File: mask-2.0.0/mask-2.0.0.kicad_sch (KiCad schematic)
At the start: 8 parts

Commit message: mask-2.0.0: basic schematic, start cleaning up the ratsnets
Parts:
- removed D?: SK6812, LED_SMD:LED_SK6812_EC15_1.5x1.5mm, symbol LED:SK6812
- added C10, C20, C21: 1uF, Capacitor_SMD:C_0603_1608Metric, symbol Device:C
- added C11, C12, C13, C14, C15, C16, C17, C18, C19, C6, C7: 100nF, Capacitor_SMD:C_0603_1608Metric, symbol Device:C
- added C2, C3: 10nF, Capacitor_SMD:C_0603_1608Metric, symbol Device:C
- added C4: 10pF, Capacitor_SMD:C_0603_1608Metric, symbol Device:C
- added C5: 10uF, Capacitor_SMD:C_0805_2012Metric, symbol Device:C
- added C8, C9: 22pF, Capacitor_SMD:C_0603_1608Metric, symbol Device:C
- added D1, D10, D11, D12, D13, D14, D15, D16, D17, D18, D19, D2, D20, D21, D22, D23, D24, D25, D26, D27, D28, D29, D3, D30, D31, D32, D33, D34, D35, D36, D37, D38, D39, D4, D40, D41, D42, D43, D44, D45, D46, D47, D48, D49, D5, D50, D51, D52, D53, D54, D55, D56, D57, D58, D59, D6, D60, D7, D8, D9: 1N4148W, Diode_SMD:D_SOD-123, symbol Diode:1N4148W
- added D61: PRTR5V0U2X, Package_TO_SOT_SMD:SOT-143, symbol Power_Protection:PRTR5V0U2X
- added D62: LED, LED_SMD:LED_0603_1608Metric, symbol Device:LED
- added FB1: 120R@550mA, Resistor_SMD:R_0603_1608Metric, symbol Device:FerriteBead
- added J2, J3: Conn_01x04, Connector_PinHeader_2.54mm:PinHeader_1x04_P2.54mm_Vertical, symbol Connector_Generic:Conn_01x04
- added R2, R3: 27, Resistor_SMD:R_0603_1608Metric, symbol Device:R
- added R4, R5: 5.1k, Resistor_SMD:R_0603_1608Metric, symbol Device:R
- added R6, R8: 10k, Resistor_SMD:R_0603_1608Metric, symbol Device:R
- added R7: 1k, Resistor_SMD:R_0603_1608Metric, symbol Device:R
- added SW1, SW10, SW11, SW12, SW13, SW14, SW15, SW16, SW17, SW18, SW19, SW2, SW20, SW21, SW22, SW23, SW24, SW25, SW26, SW27, SW28, SW29, SW3, SW30, SW31, SW32, SW33, SW34, SW35, SW36, SW37, SW38, SW39, SW4, SW40, SW41, SW42, SW43, SW44, SW45, SW46, SW47, SW48, SW49, SW5, SW50, SW51, SW52, SW53, SW54, SW55, SW56, SW57, SW58, SW59, SW6, SW60, SW7, SW8, SW9: Cherry_MX_ULP_SK6812_1515, mask:Cherry_MX_ULP_SK6812_1515, symbol mask:Cherry_MX_ULP_SK6812_1515
- added SW61, SW62: SW_Push, Button_Switch_SMD:SW_SPST_B3U-1000P, symbol Switch:SW_Push
- C1: renamed from C?; value C -> 10uF; footprint (none) -> Capacitor_SMD:C_0805_2012Metric
- R1: renamed from R?; value R -> 1k; footprint (none) -> Resistor_SMD:R_0603_1608Metric
- Y1: renamed from Y?; value Crystal -> 445C25D12M00000; Digikey https://www.digikey.at/de/products/detail/cts-frequency-controls/445C35D12M00000/3135822 -> https://www.digikey.at/de/products/detail/cts-frequency-controls/445C25D12M00000/3135096
- gave numbers to parts that had none: 4
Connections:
- net QSPI_SS: now reaches U3.1 (~{CS})
- net QSPI_SS: now also U1.56 (QSPI_SS), R6.1, R7.2
- net at U3.2 (DO(IO1)): now also U1.55 (QSPI_SD1)
- net at U3.3 (IO2): now also U1.54 (QSPI_SD2)
- net GND: now reaches U3.4 (GND)
- net GND: now also C1.2, J1.A1 (GND), J1.A12 (GND), J1.B1 (GND), J1.B12 (GND), U1.19 (TESTEN), U1.57 (GND), U2.2 (GND), C10.2, C11.2, C12.2, C13.2, C14.2, C15.2, C16.2, C17.2, C18.2, C19.2, C2.2, C20.2, C21.2, C3.2, C4.2, C5.2, C6.2, C7.2, C8.2, C9.2, D61.1 (GND), J2.4 (Pin_4), J3.4 (Pin_4), R4.2, R5.2, R8.1, SW1.1 (VSS), SW10.1 (VSS), SW11.1 (VSS), SW12.1 (VSS), SW13.1 (VSS), SW14.1 (VSS), SW15.1 (VSS), SW16.1 (VSS), SW17.1 (VSS), SW18.1 (VSS), SW19.1 (VSS), SW2.1 (VSS), SW20.1 (VSS), SW21.1 (VSS), SW22.1 (VSS), SW23.1 (VSS), SW24.1 (VSS), SW25.1 (VSS), SW26.1 (VSS), SW27.1 (VSS), SW28.1 (VSS), SW29.1 (VSS), SW3.1 (VSS), SW30.1 (VSS), SW31.1 (VSS), SW32.1 (VSS), SW33.1 (VSS), SW34.1 (VSS), SW35.1 (VSS), SW36.1 (VSS), SW37.1 (VSS), SW38.1 (VSS), SW39.1 (VSS), SW4.1 (VSS), SW40.1 (VSS), SW41.1 (VSS), SW42.1 (VSS), SW43.1 (VSS), SW44.1 (VSS), SW45.1 (VSS), SW46.1 (VSS), SW47.1 (VSS), SW48.1 (VSS), SW49.1 (VSS), SW5.1 (VSS), SW50.1 (VSS), SW51.1 (VSS), SW52.1 (VSS), SW53.1 (VSS), SW54.1 (VSS), SW55.1 (VSS), SW56.1 (VSS), SW57.1 (VSS), SW58.1 (VSS), SW59.1 (VSS), SW6.1 (VSS), SW60.1 (VSS), SW61.1, SW62.1, SW7.1 (VSS), SW8.1 (VSS), SW9.1 (VSS)
- net at U3.5 (DI(IO0)): now also U1.53 (QSPI_SD0)
- net at U3.6 (CLK): now also U1.52 (QSPI_SCLK)
- net at U3.7 (IO3): now also U1.51 (QSPI_SD3)
- net +3.3V: now reaches U3.8 (VCC)
- net +3.3V: now also U1.1 (IOVDD), U1.10 (IOVDD), U1.22 (IOVDD), U1.33 (IOVDD), U1.42 (IOVDD), U1.43 (ADC_AVDD), U1.44 (VREG_IN), U1.48 (USB_VDD), U1.49 (IOVDD), U2.5 (VOUT), C13.1, C14.1, C15.1, C16.1, C17.1, C18.1, C19.1, C20.1, C21.1, C5.1, C6.1, C7.1, D62.2 (A), J2.3 (Pin_3), J3.1 (Pin_1), R6.2, SW1.3 (VDD), SW10.3 (VDD), SW11.3 (VDD), SW12.3 (VDD), SW13.3 (VDD), SW14.3 (VDD), SW15.3 (VDD), SW16.3 (VDD), SW17.3 (VDD), SW18.3 (VDD), SW19.3 (VDD), SW2.3 (VDD), SW20.3 (VDD), SW21.3 (VDD), SW22.3 (VDD), SW23.3 (VDD), SW24.3 (VDD), SW25.3 (VDD), SW26.3 (VDD), SW27.3 (VDD), SW28.3 (VDD), SW29.3 (VDD), SW3.3 (VDD), SW30.3 (VDD), SW31.3 (VDD), SW32.3 (VDD), SW33.3 (VDD), SW34.3 (VDD), SW35.3 (VDD), SW36.3 (VDD), SW37.3 (VDD), SW38.3 (VDD), SW39.3 (VDD), SW4.3 (VDD), SW40.3 (VDD), SW41.3 (VDD), SW42.3 (VDD), SW43.3 (VDD), SW44.3 (VDD), SW45.3 (VDD), SW46.3 (VDD), SW47.3 (VDD), SW48.3 (VDD), SW49.3 (VDD), SW5.3 (VDD), SW50.3 (VDD), SW51.3 (VDD), SW52.3 (VDD), SW53.3 (VDD), SW54.3 (VDD), SW55.3 (VDD), SW56.3 (VDD), SW57.3 (VDD), SW58.3 (VDD), SW59.3 (VDD), SW6.3 (VDD), SW60.3 (VDD), SW7.3 (VDD), SW8.3 (VDD), SW9.3 (VDD)
- net at Y1.1: now also R1.1, C9.1
- net at Y1.2: now also U1.20 (XIN), C8.1
- net at R1.2: now also U1.21 (XOUT)
- net USBBOOT: now reaches U1.14 (GPIO11)
- net USBBOOT: now also R7.1, SW61.2
- net SDA: now reaches U1.15 (GPIO12)
- net SDA: now also J2.1 (Pin_1)
- net SCL: now reaches U1.16 (GPIO13)
- net SCL: now also J2.2 (Pin_2)
- net +1V1: now reaches U1.23 (DVDD), U1.50 (DVDD)
- net +1V1: now also U1.45 (VREG_VOUT), C10.1, C11.1, C12.1
- net at U1.24 (SWCLK): now also J3.2 (Pin_2)
- net at U1.25 (SWD): now also J3.3 (Pin_3)
- net nRESET: now reaches U1.26 (RUN)
- net nRESET: now also SW62.2
- net LED: now reaches U1.28 (GPIO17)
- net LED: now also SW1.2 (DIN)
- net at U1.46 (USB_DM): now also R3.1
- net at U1.47 (USB_DP): now also R2.2
- net +5V: now reaches C1.1
- net +5V: now also U2.1 (VIN), U2.3 (EN), C3.1, C4.1, FB1.2
- net VBUS: now reaches J1.A4 (VBUS), J1.A9 (VBUS), J1.B4 (VBUS), J1.B9 (VBUS)
- net VBUS: now also C2.1, D61.4 (VCC), FB1.1
- net at J1.A5 (CC1): now also R5.1
- net D+: now reaches J1.A6 (D+)
- net D+: now also J1.B6 (D+), D61.2 (I/O1), R2.1
- net D-: now reaches J1.A7 (D-)
- net D-: now also J1.B7 (D-), D61.3 (I/O2), R3.2
- net at J1.B5 (CC2): now also R4.1
- new net: D35.2 (A), SW35.6
- new net: SW57.4 (DOUT), SW58.2 (DIN)
- new net: SW58.4 (DOUT), SW59.2 (DIN)
- new net: D15.2 (A), SW15.6
- new net: SW59.4 (DOUT), SW60.2 (DIN)
- new net: SW53.4 (DOUT), SW54.2 (DIN)
- new net: SW54.4 (DOUT), SW55.2 (DIN)
- new net: D50.2 (A), SW50.6
- new net: D6.2 (A), SW6.6
- new net: D12.2 (A), SW12.6
- new net: SW11.4 (DOUT), SW12.2 (DIN)
- new net: SW12.4 (DOUT), SW13.2 (DIN)
- new net: D57.2 (A), SW57.6
- new net: SW38.4 (DOUT), SW39.2 (DIN)
- new net: SW39.4 (DOUT), SW40.2 (DIN)
- new net: D53.2 (A), SW53.6
- new net: D52.2 (A), SW52.6
- new net: SW5.4 (DOUT), SW6.2 (DIN)
- new net: SW6.4 (DOUT), SW7.2 (DIN)
- new net: SW33.4 (DOUT), SW34.2 (DIN)
- new net: SW34.4 (DOUT), SW35.2 (DIN)
- new net: D17.2 (A), SW17.6
- new net: SW18.4 (DOUT), SW19.2 (DIN)
- new net: SW19.4 (DOUT), SW20.2 (DIN)
- new net: SW22.4 (DOUT), SW23.2 (DIN)
- new net: SW23.4 (DOUT), SW24.2 (DIN)
- new net: SW21.4 (DOUT), SW22.2 (DIN)
- new net: D29.2 (A), SW29.6
- new net: D1.2 (A), SW1.6
- new net: D14.2 (A), SW14.6
- new net: D22.2 (A), SW22.6
- new net: D28.2 (A), SW28.6
- new net: D40.2 (A), SW40.6
- new net: D36.2 (A), SW36.6
- new net: D16.2 (A), SW16.6
- new net: SW10.4 (DOUT), SW11.2 (DIN)
- new net: SW28.4 (DOUT), SW29.2 (DIN)
- new net: SW29.4 (DOUT), SW30.2 (DIN)
- new net: SW1.4 (DOUT), SW2.2 (DIN)
- new net: SW2.4 (DOUT), SW3.2 (DIN)
- new net: D3.2 (A), SW3.6
- new net: SW41.4 (DOUT), SW42.2 (DIN)
- new net: SW42.4 (DOUT), SW43.2 (DIN)
- new net: SW37.4 (DOUT), SW38.2 (DIN)
- new net: D24.2 (A), SW24.6
- new net: SW24.4 (DOUT), SW25.2 (DIN)
- new net: SW25.4 (DOUT), SW26.2 (DIN)
- new net: SW30.4 (DOUT), SW31.2 (DIN)
- new net: SW31.4 (DOUT), SW32.2 (DIN)
- new net: SW51.4 (DOUT), SW52.2 (DIN)
- new net: SW52.4 (DOUT), SW53.2 (DIN)
- new net: D7.2 (A), SW7.6
- new net: D43.2 (A), SW43.6
- new net: SW49.4 (DOUT), SW50.2 (DIN)
- new net: SW50.4 (DOUT), SW51.2 (DIN)
- new net: SW55.4 (DOUT), SW56.2 (DIN)
- new net: SW56.4 (DOUT), SW57.2 (DIN)
- new net: D62.1 (K), R8.2
- new net: D26.2 (A), SW26.6
- new net: D10.2 (A), SW10.6
- new net: D8.2 (A), SW8.6
- new net: D25.2 (A), SW25.6
- new net: D23.2 (A), SW23.6
- new net: D38.2 (A), SW38.6
- new net: D4.2 (A), SW4.6
- new net: D33.2 (A), SW33.6
- new net: D45.2 (A), SW45.6
- new net: SW35.4 (DOUT), SW36.2 (DIN)
- new net: D56.2 (A), SW56.6
- new net: SW48.4 (DOUT), SW49.2 (DIN)
- new net: D13.2 (A), SW13.6
- new net: D27.2 (A), SW27.6
- new net: D34.2 (A), SW34.6
- new net: D20.2 (A), SW20.6
- new net: D51.2 (A), SW51.6
- new net: D11.2 (A), SW11.6
- new net: D21.2 (A), SW21.6
- new net: SW26.4 (DOUT), SW27.2 (DIN)
- new net: SW27.4 (DOUT), SW28.2 (DIN)
- new net: SW45.4 (DOUT), SW46.2 (DIN)
- new net: SW46.4 (DOUT), SW47.2 (DIN)
- new net: SW7.4 (DOUT), SW8.2 (DIN)
- new net: D5.2 (A), SW5.6
- new net: SW8.4 (DOUT), SW9.2 (DIN)
- new net: SW10.2 (DIN), SW9.4 (DOUT)
- new net: D48.2 (A), SW48.6
- new net: D30.2 (A), SW30.6
- new net: SW43.4 (DOUT), SW44.2 (DIN)
- new net: SW44.4 (DOUT), SW45.2 (DIN)
- new net: D31.2 (A), SW31.6
- new net: D9.2 (A), SW9.6
- new net: SW16.4 (DOUT), SW17.2 (DIN)
- new net: SW17.4 (DOUT), SW18.2 (DIN)
- new net: SW3.4 (DOUT), SW4.2 (DIN)
- new net: D32.2 (A), SW32.6
- new net: D2.2 (A), SW2.6
- new net: D41.2 (A), SW41.6
- new net: D37.2 (A), SW37.6
- new net: D47.2 (A), SW47.6
- new net: SW20.4 (DOUT), SW21.2 (DIN)
- new net: SW40.4 (DOUT), SW41.2 (DIN)
- new net: D54.2 (A), SW54.6
- new net: D19.2 (A), SW19.6
- new net: D49.2 (A), SW49.6
- new net: D44.2 (A), SW44.6
- new net: D55.2 (A), SW55.6
- new net: SW13.4 (DOUT), SW14.2 (DIN)
- new net: D18.2 (A), SW18.6
- new net: D39.2 (A), SW39.6
- new net: D59.2 (A), SW59.6
- new net: SW36.4 (DOUT), SW37.2 (DIN)
- new net: SW47.4 (DOUT), SW48.2 (DIN)
- new net: D60.2 (A), SW60.6
- new net: SW14.4 (DOUT), SW15.2 (DIN)
- new net: D42.2 (A), SW42.6
- new net: SW32.4 (DOUT), SW33.2 (DIN)
- new net: D46.2 (A), SW46.6
- new net: SW15.4 (DOUT), SW16.2 (DIN)
- new net: D58.2 (A), SW58.6
- new net: SW4.4 (DOUT), SW5.2 (DIN)
- new net COL0: SW1.5, SW13.5, SW25.5, SW37.5, SW49.5
- new net COL1: SW14.5, SW2.5, SW26.5, SW38.5, SW50.5
- new net COL10: SW11.5, SW23.5, SW35.5, SW47.5, SW59.5
- new net COL11: SW12.5, SW24.5, SW36.5, SW48.5, SW60.5
- new net COL2: SW15.5, SW27.5, SW3.5, SW39.5, SW51.5
- new net COL3: SW16.5, SW28.5, SW4.5, SW40.5, SW52.5
- new net COL4: SW17.5, SW29.5, SW41.5, SW5.5, SW53.5
- new net COL5: SW18.5, SW30.5, SW42.5, SW54.5, SW6.5
- new net COL6: SW19.5, SW31.5, SW43.5, SW55.5, SW7.5
- new net COL7: SW20.5, SW32.5, SW44.5, SW56.5, SW8.5
- new net COL8: SW21.5, SW33.5, SW45.5, SW57.5, SW9.5
- new net COL9: SW10.5, SW22.5, SW34.5, SW46.5, SW58.5
- new net ROW0: D1.1 (K), D10.1 (K), D11.1 (K), D12.1 (K), D2.1 (K), D3.1 (K), D4.1 (K), D5.1 (K), D6.1 (K), D7.1 (K), D8.1 (K), D9.1 (K)
- new net ROW1: D13.1 (K), D14.1 (K), D15.1 (K), D16.1 (K), D17.1 (K), D18.1 (K), D19.1 (K), D20.1 (K), D21.1 (K), D22.1 (K), D23.1 (K), D24.1 (K)
- new net ROW2: D25.1 (K), D26.1 (K), D27.1 (K), D28.1 (K), D29.1 (K), D30.1 (K), D31.1 (K), D32.1 (K), D33.1 (K), D34.1 (K), D35.1 (K), D36.1 (K)
- new net ROW3: D37.1 (K), D38.1 (K), D39.1 (K), D40.1 (K), D41.1 (K), D42.1 (K), D43.1 (K), D44.1 (K), D45.1 (K), D46.1 (K), D47.1 (K), D48.1 (K)
- new net ROW4: D49.1 (K), D50.1 (K), D51.1 (K), D52.1 (K), D53.1 (K), D54.1 (K), D55.1 (K), D56.1 (K), D57.1 (K), D58.1 (K), D59.1 (K), D60.1 (K)
- no-connect marks 0 -> 3
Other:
- moved on the sheet: C1, J1, R1, U1, U2, U3, Y1

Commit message: mask-2.0.0: update to smd kb2040 variant
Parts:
- removed C10, C20, C21: 1uF, Capacitor_SMD:C_0603_1608Metric, symbol Device:C
- removed C11, C12, C13, C14, C15, C16, C17, C18, C19, C6, C7: 100nF, Capacitor_SMD:C_0603_1608Metric, symbol Device:C
- removed C3: 10nF, Capacitor_SMD:C_0603_1608Metric, symbol Device:C
- removed C4: 10pF, Capacitor_SMD:C_0603_1608Metric, symbol Device:C
- removed C5: 10uF, Capacitor_SMD:C_0805_2012Metric, symbol Device:C
- removed C8, C9: 22pF, Capacitor_SMD:C_0603_1608Metric, symbol Device:C
- removed D10, D11, D12, D19, D20, D21, D22, D23, D24, D31, D32, D33, D34, D35, D36, D43, D44, D45, D46, D47, D48, D55, D56, D57, D58, D59, D60, D7, D8, D9: 1N4148W, Diode_SMD:D_SOD-123, symbol Diode:1N4148W
- removed D61: PRTR5V0U2X, Package_TO_SOT_SMD:SOT-143, symbol Power_Protection:PRTR5V0U2X
- removed D62: LED, LED_SMD:LED_0603_1608Metric, symbol Device:LED
- removed FB1: 120R@550mA, Resistor_SMD:R_0603_1608Metric, symbol Device:FerriteBead
- removed J3: Conn_01x04, Connector_PinHeader_2.54mm:PinHeader_1x04_P2.54mm_Vertical, symbol Connector_Generic:Conn_01x04
- removed SW10, SW11, SW12, SW19, SW20, SW21, SW22, SW23, SW24, SW31, SW32, SW33, SW34, SW35, SW36, SW43, SW44, SW45, SW46, SW47, SW48, SW55, SW56, SW57, SW58, SW59, SW60, SW7, SW8, SW9: Cherry_MX_ULP_SK6812_1515, mask:Cherry_MX_ULP_SK6812_1515, symbol mask:Cherry_MX_ULP_SK6812_1515
- removed SW61: SW_Push, Button_Switch_SMD:SW_SPST_B3U-1000P, symbol Switch:SW_Push
- removed U1: RP2040, Package_DFN_QFN:QFN-56-1EP_7x7mm_P0.4mm_EP3.2x3.2mm, symbol MCU_RaspberryPi:RP2040
- removed U2: AP2112K-3.3, Package_TO_SOT_SMD:SOT-23-5, symbol Regulator_Linear:AP2112K-3.3
- removed U3: W25Q128JVPIQ, Package_SON:WSON-8-1EP_6x5mm_P1.27mm_EP3.4x4.3mm, symbol Memory_Flash:W25Q128JVS
- removed Y1: 445C25D12M00000, Crystal:Crystal_SMD_5032-2Pin_5.0x3.2mm, symbol Device:Crystal
- added J2: USB_C_Receptacle_USB2.0, Connector_USB:USB_C_Receptacle_JAE_DX07S016JA1R1500, symbol Connector:USB_C_Receptacle_USB2.0
- added JP1, JP2: SolderJumper_3_Bridged12, Jumper:SolderJumper-3_P1.3mm_Bridged12_RoundedPad1.0x1.5mm_NumberLabels, symbol Jumper:SolderJumper_3_Bridged12
- added JP3, JP4: SolderJumper_2_Open, Jumper:SolderJumper-2_P1.3mm_Open_RoundedPad1.0x1.5mm, symbol Jumper:SolderJumper_2_Open
- added SW26: SW_Push, Button_Switch_SMD:SW_SPST_B3U-1000P, symbol Switch:SW_Push
- added U1: ProMicro, mask:KB2040_SMD, symbol SofleKeyboard-rescue:ProMicro_2-Lily58-cache-Lily58_Pro-rescue
- C1: value 10uF -> 100nF; footprint Capacitor_SMD:C_0805_2012Metric -> Capacitor_SMD:C_0603_1608Metric
- C2: value 10nF -> 100nF
- D1, D2, D3, D4, D5, D6: footprint Diode_SMD:D_SOD-123 -> mask:D_SOD-123_TopBottom
- D10: renamed from D16; footprint Diode_SMD:D_SOD-123 -> mask:D_SOD-123_TopBottom
- D11: renamed from D17; footprint Diode_SMD:D_SOD-123 -> mask:D_SOD-123_TopBottom
- D12: renamed from D18; footprint Diode_SMD:D_SOD-123 -> mask:D_SOD-123_TopBottom
- D13: renamed from D25; footprint Diode_SMD:D_SOD-123 -> mask:D_SOD-123_TopBottom
- D14: renamed from D26; footprint Diode_SMD:D_SOD-123 -> mask:D_SOD-123_TopBottom
- D15: renamed from D27; footprint Diode_SMD:D_SOD-123 -> mask:D_SOD-123_TopBottom
- D16: renamed from D28; footprint Diode_SMD:D_SOD-123 -> mask:D_SOD-123_TopBottom
- D17: renamed from D29; footprint Diode_SMD:D_SOD-123 -> mask:D_SOD-123_TopBottom
- D18: renamed from D30; footprint Diode_SMD:D_SOD-123 -> mask:D_SOD-123_TopBottom
- D19: renamed from D37; footprint Diode_SMD:D_SOD-123 -> mask:D_SOD-123_TopBottom
- D20: renamed from D38; footprint Diode_SMD:D_SOD-123 -> mask:D_SOD-123_TopBottom
- D21: renamed from D39; footprint Diode_SMD:D_SOD-123 -> mask:D_SOD-123_TopBottom
- D22: renamed from D40; footprint Diode_SMD:D_SOD-123 -> mask:D_SOD-123_TopBottom
- D23: renamed from D41; footprint Diode_SMD:D_SOD-123 -> mask:D_SOD-123_TopBottom
- D24: renamed from D42; footprint Diode_SMD:D_SOD-123 -> mask:D_SOD-123_TopBottom
- D25: renamed from D49; footprint Diode_SMD:D_SOD-123 -> mask:D_SOD-123_TopBottom
- D26: renamed from D50; footprint Diode_SMD:D_SOD-123 -> mask:D_SOD-123_TopBottom
- D27: renamed from D51; footprint Diode_SMD:D_SOD-123 -> mask:D_SOD-123_TopBottom
- D28: renamed from D52; footprint Diode_SMD:D_SOD-123 -> mask:D_SOD-123_TopBottom
- D29: renamed from D53; footprint Diode_SMD:D_SOD-123 -> mask:D_SOD-123_TopBottom
- D30: renamed from D54; footprint Diode_SMD:D_SOD-123 -> mask:D_SOD-123_TopBottom
- D7: renamed from D13; footprint Diode_SMD:D_SOD-123 -> mask:D_SOD-123_TopBottom
- D8: renamed from D14; footprint Diode_SMD:D_SOD-123 -> mask:D_SOD-123_TopBottom
- D9: renamed from D15; footprint Diode_SMD:D_SOD-123 -> mask:D_SOD-123_TopBottom
- R2, R3: value 27 -> 1k
- R4: value 5.1k -> 1k
- R5: value 5.1k -> 2.2k
- R6, R8: value 10k -> 2.2k
- R7: value 1k -> 2.2k
- SW1, SW2, SW3, SW4, SW5, SW6: footprint mask:Cherry_MX_ULP_SK6812_1515 -> mask:Cherry_MX_ULP_SK6812_1515_TopBottom
- SW10: renamed from SW16; footprint mask:Cherry_MX_ULP_SK6812_1515 -> mask:Cherry_MX_ULP_SK6812_1515_TopBottom
- SW11: renamed from SW17; footprint mask:Cherry_MX_ULP_SK6812_1515 -> mask:Cherry_MX_ULP_SK6812_1515_TopBottom
- SW12: renamed from SW18; footprint mask:Cherry_MX_ULP_SK6812_1515 -> mask:Cherry_MX_ULP_SK6812_1515_TopBottom
- SW13: renamed from SW25; footprint mask:Cherry_MX_ULP_SK6812_1515 -> mask:Cherry_MX_ULP_SK6812_1515_TopBottom
- SW14: renamed from SW26; footprint mask:Cherry_MX_ULP_SK6812_1515 -> mask:Cherry_MX_ULP_SK6812_1515_TopBottom
- SW15: renamed from SW27; footprint mask:Cherry_MX_ULP_SK6812_1515 -> mask:Cherry_MX_ULP_SK6812_1515_TopBottom
- SW16: renamed from SW28; footprint mask:Cherry_MX_ULP_SK6812_1515 -> mask:Cherry_MX_ULP_SK6812_1515_TopBottom
- SW17: renamed from SW29; footprint mask:Cherry_MX_ULP_SK6812_1515 -> mask:Cherry_MX_ULP_SK6812_1515_TopBottom
- SW18: renamed from SW30; footprint mask:Cherry_MX_ULP_SK6812_1515 -> mask:Cherry_MX_ULP_SK6812_1515_TopBottom
- SW19: renamed from SW37; footprint mask:Cherry_MX_ULP_SK6812_1515 -> mask:Cherry_MX_ULP_SK6812_1515_TopBottom
- SW20: renamed from SW38; footprint mask:Cherry_MX_ULP_SK6812_1515 -> mask:Cherry_MX_ULP_SK6812_1515_TopBottom
- SW21: renamed from SW39; footprint mask:Cherry_MX_ULP_SK6812_1515 -> mask:Cherry_MX_ULP_SK6812_1515_TopBottom
- SW22: renamed from SW40; footprint mask:Cherry_MX_ULP_SK6812_1515 -> mask:Cherry_MX_ULP_SK6812_1515_TopBottom
- SW23: renamed from SW41; footprint mask:Cherry_MX_ULP_SK6812_1515 -> mask:Cherry_MX_ULP_SK6812_1515_TopBottom
- SW24: renamed from SW42; footprint mask:Cherry_MX_ULP_SK6812_1515 -> mask:Cherry_MX_ULP_SK6812_1515_TopBottom
- SW27: renamed from SW49; footprint mask:Cherry_MX_ULP_SK6812_1515 -> mask:Cherry_MX_ULP_SK6812_1515_TopBottom
- SW28: renamed from SW50; footprint mask:Cherry_MX_ULP_SK6812_1515 -> mask:Cherry_MX_ULP_SK6812_1515_TopBottom
- SW29: renamed from SW51; footprint mask:Cherry_MX_ULP_SK6812_1515 -> mask:Cherry_MX_ULP_SK6812_1515_TopBottom
- SW30: renamed from SW52; footprint mask:Cherry_MX_ULP_SK6812_1515 -> mask:Cherry_MX_ULP_SK6812_1515_TopBottom
- SW31: renamed from SW53; footprint mask:Cherry_MX_ULP_SK6812_1515 -> mask:Cherry_MX_ULP_SK6812_1515_TopBottom
- SW32: renamed from SW54; footprint mask:Cherry_MX_ULP_SK6812_1515 -> mask:Cherry_MX_ULP_SK6812_1515_TopBottom
- SW7: renamed from SW13; footprint mask:Cherry_MX_ULP_SK6812_1515 -> mask:Cherry_MX_ULP_SK6812_1515_TopBottom
- SW8: renamed from SW14; footprint mask:Cherry_MX_ULP_SK6812_1515 -> mask:Cherry_MX_ULP_SK6812_1515_TopBottom
- SW9: renamed from SW15; footprint mask:Cherry_MX_ULP_SK6812_1515 -> mask:Cherry_MX_ULP_SK6812_1515_TopBottom
- renumbered J2 to J3, SW62 to SW25
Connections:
- net +5V is gone; now on net GND: C1.1
- net USBBOOT is gone; now on net SDA: R7.1
- net +3.3V: now also J1.A4 (VBUS), J1.A9 (VBUS), J1.B4 (VBUS), J1.B9 (VBUS), R5.2, R7.2, R8.2, J2.A4 (VBUS), J2.A9 (VBUS), J2.B4 (VBUS), J2.B9 (VBUS), U1.21 (VCC)
- net GND: now also C2.1, R1.2, R2.2, J2.A1 (GND), J2.A12 (GND), J2.B1 (GND), J2.B12 (GND), SW26.1, U1.23 (GND), U1.3 (GND), U1.4 (GND); no longer C1.2, C2.2, R4.2, R5.2, R8.1
- net SCL: now also R5.1, R6.1, JP3.2 (B), JP4.2 (B), U1.6 (SCL(PD0))
- net SDA: now also R8.1, JP1.3 (B), JP2.3 (B), U1.5 (SDA(PD1))
- net nRESET: now also R3.2, R4.2, U1.22 (RST); no longer SW25.2
- net at R1.1: now also C1.2, C2.2, J1.S1 (SHIELD), R2.1, J2.S1 (SHIELD)
- net at SW7.2 (DIN): now also SW6.4 (DOUT)
- net at SW12.4 (DOUT): now also SW13.2 (DIN)
- net at SW24.4 (DOUT): now also SW27.2 (DIN)
- net at SW18.4 (DOUT): now also SW19.2 (DIN)
- net at R3.1: now also R4.1, SW25.2, SW26.2
- net at J1.A5 (CC1): no longer R5.1
- net at J1.B5 (CC2): no longer R4.1
- net D+ renamed SPLIT_DATA
- net SPLIT_DATA: now also J2.A6 (D+), J2.B6 (D+), JP1.2 (C), JP2.2 (C); no longer R2.1
- net D- renamed SPLIT_CLOCK
- net SPLIT_CLOCK: now also J2.A7 (D-), J2.B7 (D-), JP3.1 (A), JP4.1 (A); no longer R3.2
- net LED renamed ONEWIRE_LED
- net ONEWIRE_LED: now also U1.1 (TX(PD3))
- removed net QSPI_SS: R6.1, R7.2
- removed net VBUS: C2.1, J1.A4 (VBUS), J1.A9 (VBUS), J1.B4 (VBUS), J1.B9 (VBUS)
- new net SPLIT_DATA_UART: JP1.1 (A), JP2.1 (A), U1.2 (RX(PD2))
- no-connect marks 3 -> 6
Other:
- moved on the sheet: D1, D10, D11, D12, D13, D14, D15, D16, D17, D18, D19, D2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

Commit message: mask-2.0.0: first layout prototype
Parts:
- renumbered SW27 to SW25, SW28 to SW26, SW29 to SW27, SW30 to SW28, SW31 to SW29, SW32 to SW30, SW25 to SW31, SW26 to SW32
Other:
- moved on the sheet: R3, R4, SW31, SW32

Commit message: mask-2.0.0: routing halfway done, 3.3v for led's next
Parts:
- D1, D10, D11, D12, D13, D14, D15, D16, D17, D18, D19, D2, D20, D21, D22, D23, D24, D25, D26, D27, D28, D29, D3, D30, D4, D5, D6, D7, D8, D9: footprint mask:D_SOD-123_TopBottom -> mask:D_0603_1608Metric_TopBottom
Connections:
- net COL0: no longer SW25.5
- net COL1: no longer SW26.5
- net COL2: no longer SW27.5
- net COL3: no longer SW28.5
- net COL4: now also SW25.5; no longer SW29.5
- net COL5: now also SW26.5; no longer SW30.5
- net ONEWIRE_LED: now also SW6.2 (DIN); no longer SW1.2 (DIN)
- net ROW3: now also D29.1 (K), D30.1 (K)
- net ROW4: no longer D29.1 (K), D30.1 (K)
- net at SW30.4 (DOUT): now also SW28.2 (DIN)
- net at SW5.4 (DOUT): now also SW4.2 (DIN); no longer SW6.2 (DIN)
- net at SW6.4 (DOUT): now also SW5.2 (DIN); no longer SW7.2 (DIN)
- net at SW17.2 (DIN): now also SW18.4 (DOUT); no longer SW16.4 (DOUT)
- net at SW17.4 (DOUT): now also SW16.2 (DIN); no longer SW18.2 (DIN)
- net at SW2.2 (DIN): now also SW3.4 (DOUT); no longer SW1.4 (DOUT)
- net at SW2.4 (DOUT): now also SW1.2 (DIN); no longer SW3.2 (DIN)
- net at SW24.4 (DOUT): now also SW29.2 (DIN); no longer SW25.2 (DIN)
- net at SW13.2 (DIN): now also SW14.4 (DOUT); no longer SW12.4 (DOUT)
- net at SW13.4 (DOUT): now also SW19.2 (DIN); no longer SW14.2 (DIN)
- net at SW27.4 (DOUT): now also SW26.2 (DIN); no longer SW28.2 (DIN)
- net at SW28.4 (DOUT): now also SW27.2 (DIN); no longer SW29.2 (DIN)
- net at SW25.4 (DOUT): no longer SW26.2 (DIN)
- net at SW26.4 (DOUT): now also SW25.2 (DIN); no longer SW27.2 (DIN)
- net at SW15.2 (DIN): now also SW16.4 (DOUT); no longer SW14.4 (DOUT)
- net at SW15.4 (DOUT): now also SW14.2 (DIN); no longer SW16.2 (DIN)
- net at SW4.4 (DOUT): now also SW3.2 (DIN); no longer SW5.2 (DIN)
- new net: SW12.4 (DOUT), SW18.2 (DIN)
- new net: SW1.4 (DOUT), SW7.2 (DIN)
- new net COL6: SW27.5, SW29.5
- new net COL7: SW28.5, SW30.5
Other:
- moved on the sheet: D25, D26, D27, D28, D29, D30, SW10B, SW11B, SW12B, SW13B, SW14B, SW15B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

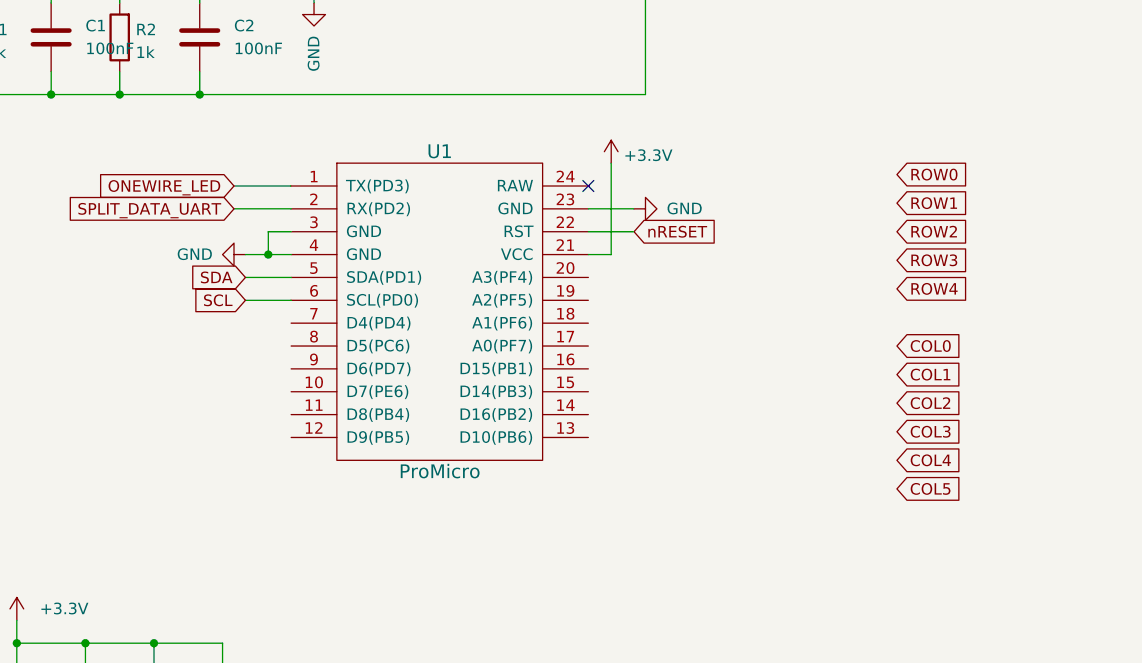
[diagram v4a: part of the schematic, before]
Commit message: mask-2.0.0: finalize routing
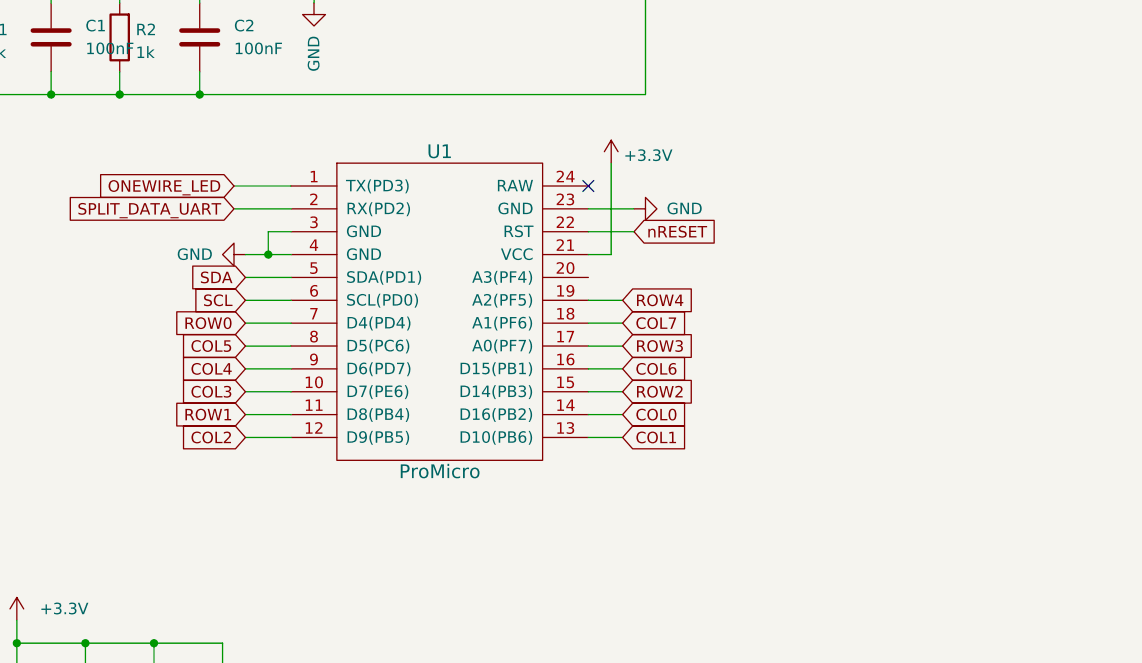
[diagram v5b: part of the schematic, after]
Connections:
- net COL0: now also U1.14 (D16(PB2))
- net COL1: now also U1.13 (D10(PB6))
- net COL2: now also U1.12 (D9(PB5))
- net COL3: now also U1.10 (D7(PE6))
- net COL4: now also U1.9 (D6(PD7))
- net COL5: now also U1.8 (D5(PC6))
- net COL6: now also U1.16 (D15(PB1))
- net COL7: now also U1.18 (A1(PF6))
- net ROW0: now also U1.7 (D4(PD4))
- net ROW1: now also U1.11 (D8(PB4))
- net ROW2: now also U1.15 (D14(PB3))
- net ROW3: now also U1.17 (A0(PF7))
- net ROW4: now also U1.19 (A2(PF5))
